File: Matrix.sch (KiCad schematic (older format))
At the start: 227 parts

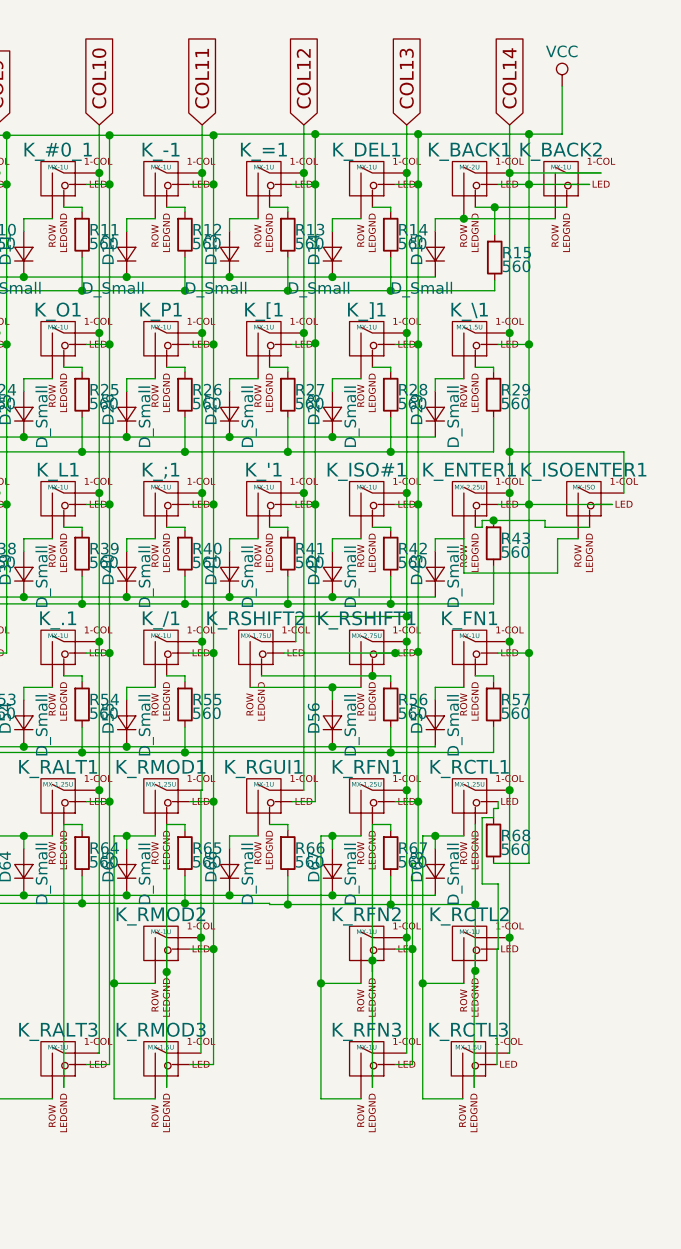
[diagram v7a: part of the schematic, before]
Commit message: Update: More routing and fix a schematic mistake
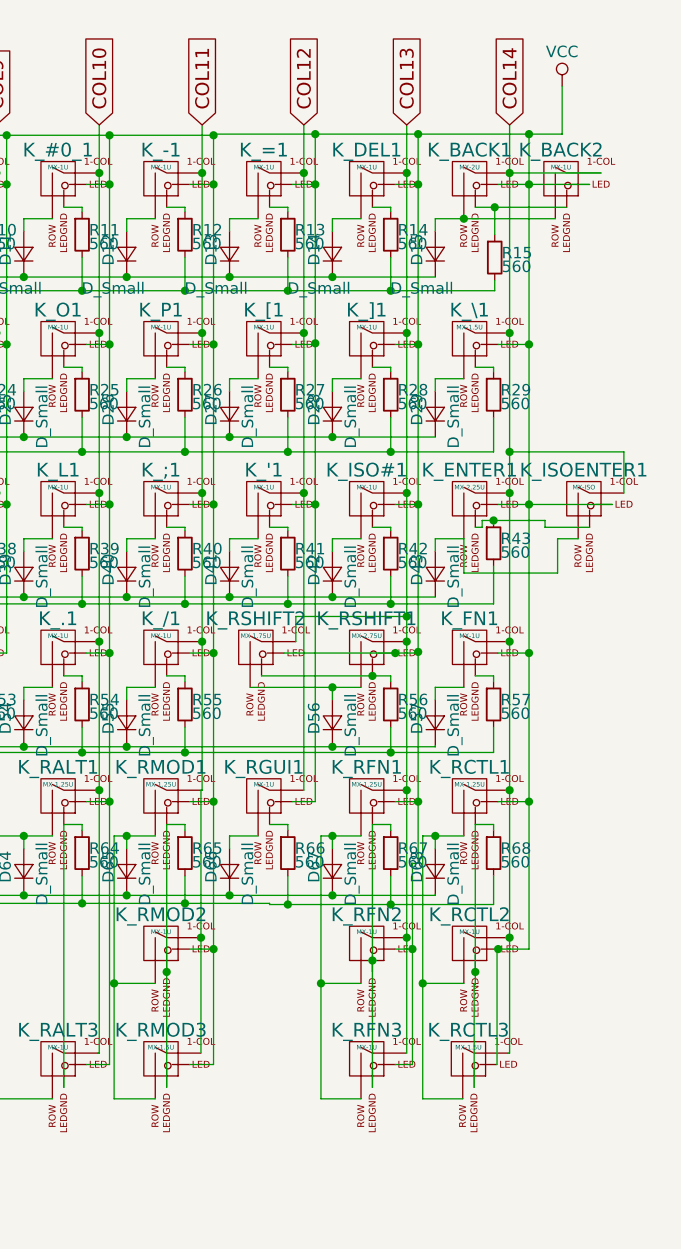
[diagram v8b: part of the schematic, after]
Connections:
- net LEDGND: now also R68.2; no longer K_RCTL1.4 (LEDGND), K_RCTL2.4 (LEDGND), K_RCTL3.4 (LEDGND)
- net VCC: now also K_RCTL1.3 (LED), K_RCTL2.3 (LED), K_RCTL3.3 (LED); no longer R68.2
- new net: K_RCTL1.4 (LEDGND), K_RCTL2.4 (LEDGND), K_RCTL3.4 (LEDGND), R68.1
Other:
- moved on the sheet: R68
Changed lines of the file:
@@
 L R_Small R68
 U 1 1 5ABB7AA6
-P 8005 3995
-F 0 "R68" H 8035 4015 50  0000 L CNN
-F 1 "560" H 8035 3955 50  0000 L CNN
-F 2 "Resistors_SMD:R_0603" H 8005 3995 50  0001 C CNN
-F 3 "" H 8005 3995 50  0001 C CNN
-	1    8005 3995
+P 8005 4050
+F 0 "R68" H 8035 4070 50  0000 L CNN
+F 1 "560" H 8035 4010 50  0000 L CNN
+F 2 "Resistors_SMD:R_0603" H 8005 4050 50  0001 C CNN
+F 3 "" H 8005 4050 50  0001 C CNN
+	1    8005 4050
 	1    0    0    -1
 $EndComp
@@
 	1    0    0    -1
 $EndComp
+$Comp
+L MX-1U K_'1
+U 1 1 5AB12477
+P 7000 2500
+F 0 "K_'1" H 7000 2625 60  0000 C CNN
+F 1 "MX-1U" H 7000 2550 20  0000 C CNN
+F 2 "MX_Alps_Hybrid:MXOnly-1U-FLIPPED" H 6975 2475 60  0001 C CNN
+F 3 "" H 6975 2475 60  0001 C CNN
+	1    7000 2500
+	1    0    0    -1
+$EndComp
+$Comp
+L MX-1.25U K_RFN1
+U 1 1 5ABB6B6D
+P 7450 3800
+F 0 "K_RFN1" H 7450 3925 60  0000 C CNN
+F 1 "MX-1.25U" H 7450 3850 20  0000 C CNN
+F 2 "MX_Alps_Hybrid:MXOnly-1.25U-FLIPPED" H 7425 3775 60  0001 C CNN
+F 3 "" H 7425 3775 60  0001 C CNN
+	1    7450 3800
+	1    0    0    -1
+$EndComp
+$Comp
+L MX-1U K_RFN2
+U 1 1 5AE3B5E8
+P 7450 4445
+F 0 "K_RFN2" H 7450 4570 60  0000 C CNN
+F 1 "MX-1U" H 7450 4495 20  0000 C CNN
+F 2 "MX_Alps_Hybrid:MXOnly-1U" H 7425 4420 60  0001 C CNN
+F 3 "" H 7425 4420 60  0001 C CNN
+	1    7450 4445
+	1    0    0    -1
+$EndComp
 Wire Wire Line
 	1655 1225 1655 1245
@@
 	4150 4030 4150 3975
 Wire Wire Line
-	8020 4470 8025 4470
-Wire Wire Line
-	8020 4975 8020 4470
+	8160 4470 8020 4470
+Wire Wire Line
+	8020 4470 8020 4975
 Connection ~ 2675 3775
 Wire Wire Line
@@
 Wire Wire Line
 	2475 4630 2310 4630
-Connection ~ 7925 4565
-Wire Wire Line
-	7925 4565 7920 4565
-Wire Wire Line
-	7920 4565 7920 5075
 Connection ~ 8075 4420
 Wire Wire Line
@@
 Connection ~ 7300 4235
 Wire Wire Line
-	8005 3895 8005 3855
-Wire Wire Line
-	8005 3855 8025 3855
-Wire Wire Line
-	8025 3855 8025 3825
-Wire Wire Line
 	1725 865  1725 4430
 Wire Wire Line
@@
 	7675 905  7675 4095
 Wire Wire Line
-	8025 4470 8025 4185
-Wire Wire Line
-	8025 4185 7955 4185
-Wire Wire Line
-	7955 4185 7955 3895
-Wire Wire Line
-	7955 3895 8005 3895
-Wire Wire Line
-	8160 4095 8005 4095
-Wire Wire Line
-	8160 905  8160 4095
+	8160 905  8160 4470
 Wire Wire Line
 	1790 910  6780 910
@@
 Connection ~ 1125 3610
 Wire Wire Line
-	7925 3925 7925 4570
-Wire Wire Line
-	7025 4275 7925 4275
+	7025 4275 8005 4275
 Wire Wire Line
 	985  4270 7025 4270
@@
 Wire Wire Line
 	545  4425 985  4425
-Connection ~ 7925 4275
 Wire Wire Line
 	1525 4630 1265 4630
@@
 	7105 4150 7105 4275
 Connection ~ 7105 4275
-$Comp
-L MX-1U K_'1
-U 1 1 5AB12477
-P 7000 2500
-F 0 "K_'1" H 7000 2625 60  0000 C CNN
-F 1 "MX-1U" H 7000 2550 20  0000 C CNN
-F 2 "MX_Alps_Hybrid:MXOnly-1U-FLIPPED" H 6975 2475 60  0001 C CNN
-F 3 "" H 6975 2475 60  0001 C CNN
-	1    7000 2500
-	1    0    0    -1
-$EndComp
 Wire Wire Line
 	7225 3825 7125 3825
-$Comp
-L MX-1.25U K_RFN1
-U 1 1 5ABB6B6D
-P 7450 3800
-F 0 "K_RFN1" H 7450 3925 60  0000 C CNN
-F 1 "MX-1.25U" H 7450 3850 20  0000 C CNN
-F 2 "MX_Alps_Hybrid:MXOnly-1.25U-FLIPPED" H 7425 3775 60  0001 C CNN
-F 3 "" H 7425 3775 60  0001 C CNN
-	1    7450 3800
-	1    0    0    -1
-$EndComp
-$Comp
-L MX-1U K_RFN2
-U 1 1 5AE3B5E8
-P 7450 4445
-F 0 "K_RFN2" H 7450 4570 60  0000 C CNN
-F 1 "MX-1U" H 7450 4495 20  0000 C CNN
-F 2 "MX_Alps_Hybrid:MXOnly-1U" H 7425 4420 60  0001 C CNN
-F 3 "" H 7425 4420 60  0001 C CNN
-	1    7450 4445
-	1    0    0    -1
-$EndComp
 Wire Wire Line
 	7475 3925 7555 3925
@@
 Connection ~ 6780 4470
 Connection ~ 6575 4570
+Wire Wire Line
+	7925 3925 8005 3925
+Wire Wire Line
+	8005 3925 8005 3950
+Wire Wire Line
+	8005 4275 8005 4150
+Wire Wire Line
+	8025 3825 8160 3825
+Connection ~ 8160 3825
+Connection ~ 8025 4470
+Wire Wire Line
+	7920 5075 7920 4625
+Wire Wire Line
+	7925 4625 7920 4625
+Wire Wire Line
+	7925 3925 7925 4625
+Connection ~ 7925 4570
 $EndSCHEMATC
